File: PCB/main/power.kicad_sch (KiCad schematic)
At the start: 16 parts, among them J2 Battery wire pads 2x 2.54mm, SW1 Off-board pack toggle switch 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, U4 XC6220B331MR-G, U6 BQ24074RGTR

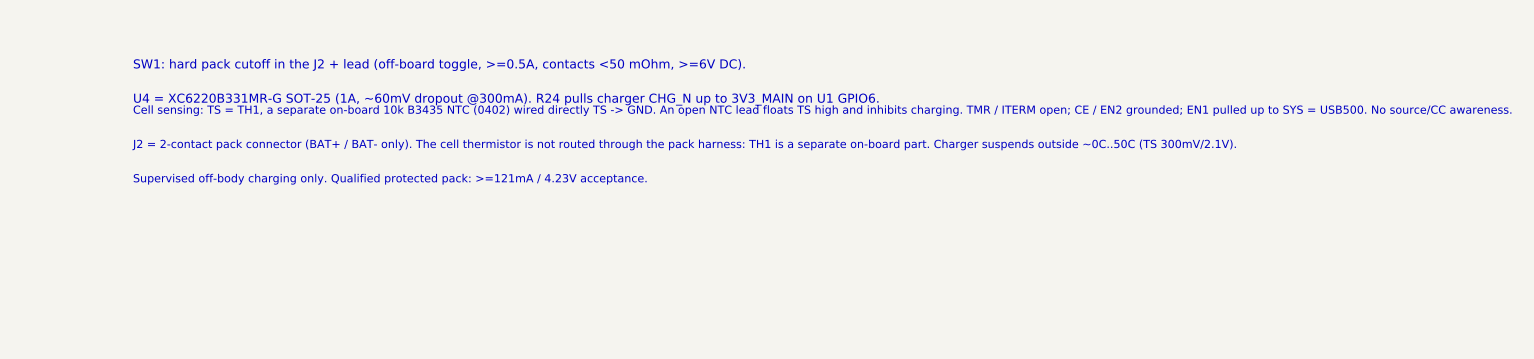
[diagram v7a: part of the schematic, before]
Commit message: fab: eliminate JLCPCB export warnings (H1-H3 mounting holes in schematic, U4 footprint aligned)
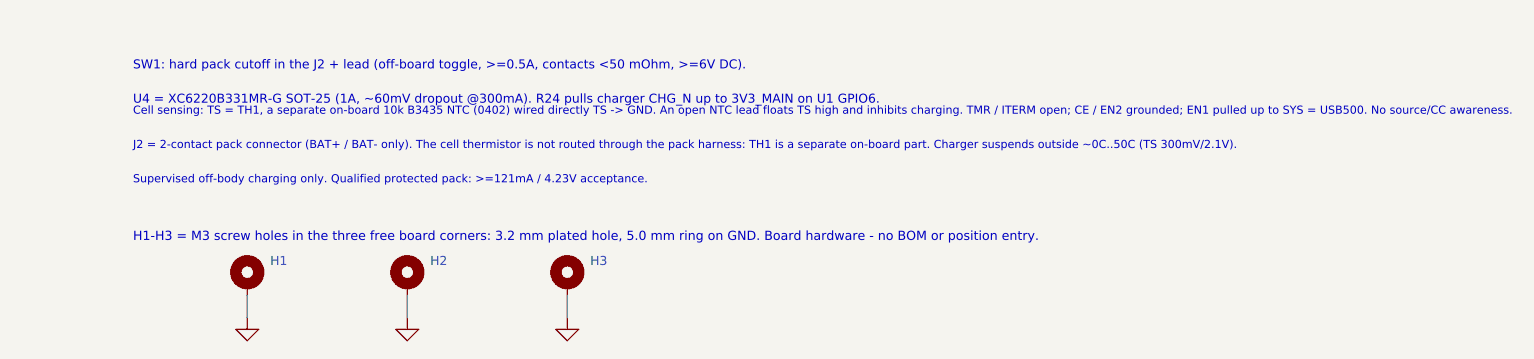
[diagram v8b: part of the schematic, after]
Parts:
- added H1, H2, H3: MountingHole_3.2mm_M3_Pad_5mm, smove-r2-main:MountingHole_3.2mm_M3_Pad_5mm, symbol smove-r2-main:MountingHole_3.2mm_M3_Pad_5mm
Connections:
- net GND: now also H1.1, H2.1, H3.1
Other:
- note added: "H1-H3 = M3 screw holes in the three free board corners: 3.2 mm plated hole, 5.0 mm ring on GND. Board hardware - no BOM or position entry."
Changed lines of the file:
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@@
         (path "/8e261347-838a-5848-981d-f693675e8aa0/a926f61e-132d-5af0-876e-12788077b17d"
           (reference "R25")
-          (unit 1))))))
+          (unit 1)))))
+  (text "H1-H3 = M3 screw holes in the three free board corners: 3.2 mm plated hole, 5.0 mm ring on GND. Board hardware - no BOM or position entry."
+    (at 25.4 184.15 0)
+    (effects
+      (font
+        (size 1.02 1.02))
+      (justify left))
+)
+  (symbol
+    (lib_id "smove-r2-main:MountingHole_3.2mm_M3_Pad_5mm")
+    (at 38.1 187.96 0)
+    (unit 1)
+    (in_bom no)
+    (on_board yes)
+    (dnp no)
+    (property "Reference" "H1"
+      (at 40.64 186.69 0)
+      (effects
+        (font
+          (size 1 1))
+        (justify left)))
+    (property "Value" "MountingHole_3.2mm_M3_Pad_5mm"
+      (at 38.1 191.77 0)
+      (effects
+        (font
+          (size 0.9 0.9))
+        (hide yes)))
+    (property "Footprint" "smove-r2-main:MountingHole_3.2mm_M3_Pad_5mm"
+      (at 38.1 187.96 0)
+      (effects
+        (font
+          (size 1 1))
+        (hide yes)))
+    (property "Description" "M3 screw mounting hole: 3.2 mm plated (PTH) clearance drill with a 5.0 mm grounded copper ring on all four copper layers and a solder-mask opening over the ring, so the screw head bears on exposed GND copper. Solid zone connection (no thermal spokes). Board hardware: pad 1 is the only electrical pin, it is wired to GND, and the part is excluded from the BOM and the position files."
+      (at 38.1 187.96 0)
+      (effects
+        (font
+          (size 1 1))
+        (hide yes)))
+    (pin "1"
+)
+    (instances
+      (project "smove-r2-main"
+        (path "/8e261347-838a-5848-981d-f693675e8aa0/a926f61e-132d-5af0-876e-12788077b17d"
+          (reference "H1")
+          (unit 1)))))
+  (wire
+    (pts
+      (xy 38.1 190.5)
+      (xy 38.1 193.04))
+    (stroke
+      (width 0)
+      (type default))
+)
+  (symbol
+    (lib_id "power:GND")
+    (at 38.1 193.04 0)
+    (unit 1)
+    (in_bom no)
+    (on_board no)
+    (dnp no)
+    (property "Reference" "#PWR28"
+      (at 38.1 185.42 0)
+      (effects
+        (font
+          (size 1 1))
+        (hide yes)))
+    (property "Value" "GND"
+      (at 38.1 188.976 0)
+      (effects
+        (font
+          (size 0.95 0.95))
+        (hide yes)))
+    (pin "1"
+)
+    (instances
+      (project "smove-r2-main"
+        (path "/8e261347-838a-5848-981d-f693675e8aa0/a926f61e-132d-5af0-876e-12788077b17d"
+          (reference "#PWR28")
+          (unit 1)))))
+  (symbol
+    (lib_id "smove-r2-main:MountingHole_3.2mm_M3_Pad_5mm")
+    (at 55.88 187.96 0)
+    (unit 1)
+    (in_bom no)
+    (on_board yes)
+    (dnp no)
+    (property "Reference" "H2"
+      (at 58.42 186.69 0)
+      (effects
+        (font
+          (size 1 1))
+        (justify left)))
+    (property "Value" "MountingHole_3.2mm_M3_Pad_5mm"
+      (at 55.88 191.77 0)
+      (effects
+        (font
+          (size 0.9 0.9))
+        (hide yes)))
+    (property "Footprint" "smove-r2-main:MountingHole_3.2mm_M3_Pad_5mm"
+      (at 55.88 187.96 0)
+      (effects
+        (font
+          (size 1 1))
+        (hide yes)))
+    (property "Description" "M3 screw mounting hole: 3.2 mm plated (PTH) clearance drill with a 5.0 mm grounded copper ring on all four copper layers and a solder-mask opening over the ring, so the screw head bears on exposed GND copper. Solid zone connection (no thermal spokes). Board hardware: pad 1 is the only electrical pin, it is wired to GND, and the part is excluded from the BOM and the position files."
+      (at 55.88 187.96 0)
+      (effects
+        (font
+          (size 1 1))
+        (hide yes)))
+    (pin "1"
+)
+    (instances
+      (project "smove-r2-main"
+        (path "/8e261347-838a-5848-981d-f693675e8aa0/a926f61e-132d-5af0-876e-12788077b17d"
+          (reference "H2")
+          (unit 1)))))
+  (wire
+    (pts
+      (xy 55.88 190.5)
+      (xy 55.88 193.04))
+    (stroke
+      (width 0)
+      (type default))
+)
+  (symbol
+    (lib_id "power:GND")
+    (at 55.88 193.04 0)
+    (unit 1)
+    (in_bom no)
+    (on_board no)
+    (dnp no)
+    (property "Reference" "#PWR29"
+      (at 55.88 185.42 0)
+      (effects
+        (font
+          (size 1 1))
+        (hide yes)))
+    (property "Value" "GND"
+      (at 55.88 188.976 0)
+      (effects
+        (font
+          (size 0.95 0.95))
+        (hide yes)))
+    (pin "1"
+)
+    (instances
+      (project "smove-r2-main"
+        (path "/8e261347-838a-5848-981d-f693675e8aa0/a926f61e-132d-5af0-876e-12788077b17d"
+          (reference "#PWR29")
+          (unit 1)))))
+  (symbol
+    (lib_id "smove-r2-main:MountingHole_3.2mm_M3_Pad_5mm")
+    (at 73.66 187.96 0)
+    (unit 1)
+    (in_bom no)
+    (on_board yes)
+    (dnp no)
+    (property "Reference" "H3"
+      (at 76.2 186.69 0)
+      (effects
+        (font
+          (size 1 1))
+        (justify left)))
+    (property "Value" "MountingHole_3.2mm_M3_Pad_5mm"
+      (at 73.66 191.77 0)
+      (effects
+        (font
+          (size 0.9 0.9))
+        (hide yes)))
+    (property "Footprint" "smove-r2-main:MountingHole_3.2mm_M3_Pad_5mm"
+      (at 73.66 187.96 0)
+      (effects
+        (font
+          (size 1 1))
+        (hide yes)))
+    (property "Description" "M3 screw mounting hole: 3.2 mm plated (PTH) clearance drill with a 5.0 mm grounded copper ring on all four copper layers and a solder-mask opening over the ring, so the screw head bears on exposed GND copper. Solid zone connection (no thermal spokes). Board hardware: pad 1 is the only electrical pin, it is wired to GND, and the part is excluded from the BOM and the position files."
+      (at 73.66 187.96 0)
+      (effects
+        (font
+          (size 1 1))
+        (hide yes)))
+    (pin "1"
+)
+    (instances
+      (project "smove-r2-main"
+        (path "/8e261347-838a-5848-981d-f693675e8aa0/a926f61e-132d-5af0-876e-12788077b17d"
+          (reference "H3")
+          (unit 1)))))
+  (wire
+    (pts
+      (xy 73.66 190.5)
+      (xy 73.66 193.04))
+    (stroke
+      (width 0)
+      (type default))
+)
+  (symbol
+    (lib_id "power:GND")
+    (at 73.66 193.04 0)
+    (unit 1)
+    (in_bom no)
+    (on_board no)
+    (dnp no)
+    (property "Reference" "#PWR30"
+      (at 73.66 185.42 0)
+      (effects
+        (font
+          (size 1 1))
+        (hide yes)))
+    (property "Value" "GND"
+      (at 73.66 188.976 0)
+      (effects
+        (font
+          (size 0.95 0.95))
+        (hide yes)))
+    (pin "1"
+)
+    (instances
+      (project "smove-r2-main"
+        (path "/8e261347-838a-5848-981d-f693675e8aa0/a926f61e-132d-5af0-876e-12788077b17d"
+          (reference "#PWR30")
+          (unit 1)))))
+)
